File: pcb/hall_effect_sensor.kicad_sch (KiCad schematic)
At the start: 4 parts, among them U3 TMAG5273A2QDBV

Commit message: add top level schem and cleanup
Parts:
- renumbered C19 to C21, C18 to C22, R7 to R38, U3 to U5
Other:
- note removed: "1"
- note removed: "10/27/26"
- note removed: "Hall Effect w/ I2C connection"
- note removed: "Topher Fontana"
- title: (none) -> Hall Effect Sensor
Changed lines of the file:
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@@
 	(generator_version "10.0")
 	(paper "A4")
-	(text "10/27/26"
-		(exclude_from_sim no)
-		(at 212.598 193.294 0)
-		(effects
-			(font
-				(size 1.27 1.27)
-			)
-		)
-	)
-	(text "1"
-		(exclude_from_sim no)
-		(at 270.256 193.04 0)
-		(effects
-			(font
-				(size 1.27 1.27)
-			)
-		)
-	)
-	(text "Hall Effect w/ I2C connection"
-		(exclude_from_sim no)
-		(at 201.676 189.992 0)
-		(effects
-			(font
-				(size 1.27 1.27)
-			)
-		)
-	)
-	(text "Topher Fontana"
-		(exclude_from_sim no)
-		(at 194.056 174.244 0)
-		(effects
-			(font
-				(size 2.54 2.54)
-			)
-		)
+	(title_block
+		(title "Hall Effect Sensor")
+		(date "2026-10-27")
 	)
 	(junction
@@
 		)
 		(instances
+			(project "Onboard_Project"
+				(path "/17df1232-b180-49eb-a49c-63e4861e42e5/ac3adca3-c805-4f5b-864e-01bcaec77989"
+					(reference "#PWR060")
+					(unit 1)
+				)
+			)
+			(project "hall"
+				(path "/2f82c136-670b-48e5-bbb2-95c40d4f7cdb"
+					(reference "#PWR060")
+					(unit 1)
+				)
+			)
 			(project "Onboadrd_Project"
 				(path "/b0bfccf7-bea7-4d4b-a08d-f08cc4250cda"
@@
 		)
 		(instances
+			(project "Onboard_Project"
+				(path "/17df1232-b180-49eb-a49c-63e4861e42e5/ac3adca3-c805-4f5b-864e-01bcaec77989"
+					(reference "#PWR062")
+					(unit 1)
+				)
+			)
+			(project "hall"
+				(path "/2f82c136-670b-48e5-bbb2-95c40d4f7cdb"
+					(reference "#PWR062")
+					(unit 1)
+				)
+			)
 			(project "Onboadrd_Project"
 				(path "/b0bfccf7-bea7-4d4b-a08d-f08cc4250cda"
@@
 		)
 		(instances
+			(project "Onboard_Project"
+				(path "/17df1232-b180-49eb-a49c-63e4861e42e5/ac3adca3-c805-4f5b-864e-01bcaec77989"
+					(reference "#PWR058")
+					(unit 1)
+				)
+			)
+			(project "hall"
+				(path "/2f82c136-670b-48e5-bbb2-95c40d4f7cdb"
+					(reference "#PWR058")
+					(unit 1)
+				)
+			)
 			(project "Onboadrd_Project"
 				(path "/b0bfccf7-bea7-4d4b-a08d-f08cc4250cda"
@@
 		(in_pos_files yes)
 		(dnp no)
-		(property "Reference" "C19"
+		(property "Reference" "C21"
 			(at 161.29 68.58 0)
 			(show_name no)
@@
 		)
 		(instances
+			(project "Onboard_Project"
+				(path "/17df1232-b180-49eb-a49c-63e4861e42e5/ac3adca3-c805-4f5b-864e-01bcaec77989"
+					(reference "C21")
+					(unit 1)
+				)
+			)
+			(project "hall"
+				(path "/2f82c136-670b-48e5-bbb2-95c40d4f7cdb"
+					(reference "C22")
+					(unit 1)
+				)
+			)
 			(project "Onboadrd_Project"
 				(path "/b0bfccf7-bea7-4d4b-a08d-f08cc4250cda"
@@
 		)
 		(instances
+			(project "Onboard_Project"
+				(path "/17df1232-b180-49eb-a49c-63e4861e42e5/ac3adca3-c805-4f5b-864e-01bcaec77989"
+					(reference "#PWR061")
+					(unit 1)
+				)
+			)
+			(project "hall"
+				(path "/2f82c136-670b-48e5-bbb2-95c40d4f7cdb"
+					(reference "#PWR061")
+					(unit 1)
+				)
+			)
 			(project "Onboadrd_Project"
 				(path "/b0bfccf7-bea7-4d4b-a08d-f08cc4250cda"
@@
 		)
 		(instances
+			(project "Onboard_Project"
+				(path "/17df1232-b180-49eb-a49c-63e4861e42e5/ac3adca3-c805-4f5b-864e-01bcaec77989"
+					(reference "#PWR059")
+					(unit 1)
+				)
+			)
+			(project "hall"
+				(path "/2f82c136-670b-48e5-bbb2-95c40d4f7cdb"
+					(reference "#PWR059")
+					(unit 1)
+				)
+			)
 			(project "Onboadrd_Project"
 				(path "/b0bfccf7-bea7-4d4b-a08d-f08cc4250cda"
@@
 		(dnp no)
 		(fields_autoplaced yes)
-		(property "Reference" "R7"
+		(property "Reference" "R38"
 			(at 176.53 93.9799 0)
 			(show_name no)
@@
 		)
 		(instances
+			(project "Onboard_Project"
+				(path "/17df1232-b180-49eb-a49c-63e4861e42e5/ac3adca3-c805-4f5b-864e-01bcaec77989"
+					(reference "R38")
+					(unit 1)
+				)
+			)
+			(project "hall"
+				(path "/2f82c136-670b-48e5-bbb2-95c40d4f7cdb"
+					(reference "R36")
+					(unit 1)
+				)
+			)
 			(project "Onboadrd_Project"
 				(path "/b0bfccf7-bea7-4d4b-a08d-f08cc4250cda"
@@
 		(in_pos_files yes)
 		(dnp no)
-		(property "Reference" "U3"
+		(property "Reference" "U5"
 			(at 141.478 81.28 0)
 			(show_name no)
@@
 		)
 		(instances
+			(project "Onboard_Project"
+				(path "/17df1232-b180-49eb-a49c-63e4861e42e5/ac3adca3-c805-4f5b-864e-01bcaec77989"
+					(reference "U5")
+					(unit 1)
+				)
+			)
+			(project "hall"
+				(path "/2f82c136-670b-48e5-bbb2-95c40d4f7cdb"
+					(reference "U5")
+					(unit 1)
+				)
+			)
 			(project "Onboadrd_Project"
 				(path "/b0bfccf7-bea7-4d4b-a08d-f08cc4250cda"
@@
 		(dnp no)
 		(fields_autoplaced yes)
-		(property "Reference" "C18"
+		(property "Reference" "C22"
 			(at 161.2899 81.28 0)
 			(show_name no)
@@
 		)
 		(instances
+			(project "Onboard_Project"
+				(path "/17df1232-b180-49eb-a49c-63e4861e42e5/ac3adca3-c805-4f5b-864e-01bcaec77989"
+					(reference "C22")
+					(unit 1)
+				)
+			)
+			(project "hall"
+				(path "/2f82c136-670b-48e5-bbb2-95c40d4f7cdb"
+					(reference "C23")
+					(unit 1)
+				)
+			)
 			(project "Onboadrd_Project"
 				(path "/b0bfccf7-bea7-4d4b-a08d-f08cc4250cda"
@@
 		)
 	)
-	(sheet_instances
-		(path "/"
-			(page "4")
-		)
-	)

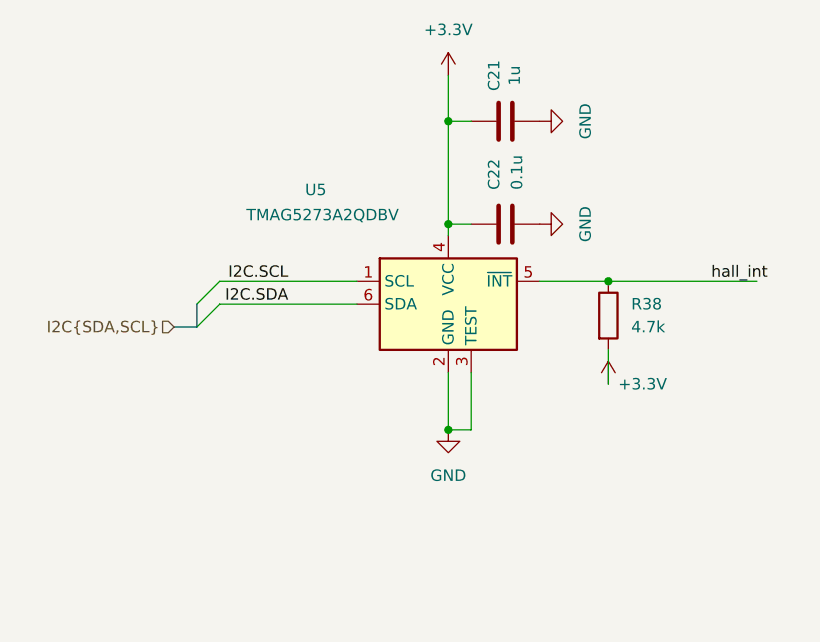
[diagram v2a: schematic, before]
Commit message: custom symbols for all ics
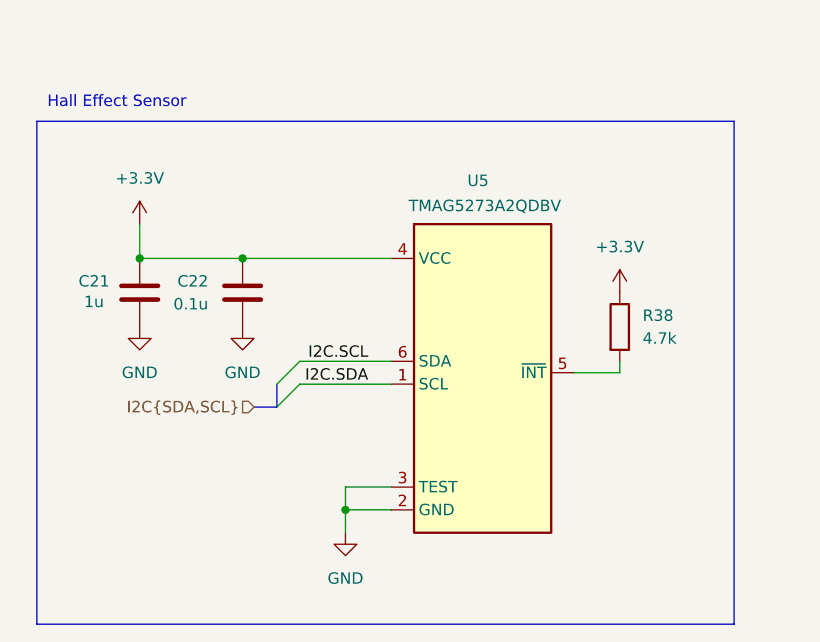
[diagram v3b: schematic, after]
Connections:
- net +3.3V: now also R38.1; no longer R38.2
- net I2C.SCL: now also U5.6 (SDA); no longer U5.1 (SCL)
- net I2C.SDA: now also U5.1 (SCL); no longer U5.6 (SDA)
- net hall_int: no longer names the net of U5.5 (~{INT})
- net hall_int: now also R38.2; no longer R38.1
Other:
- note added: "Hall Effect Sensor"
- moved on the sheet: R38, U5

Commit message: Adding some docs
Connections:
- net hall_int: now reaches R38.2, U5.5 (~{INT})

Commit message: Adding docs for GPIO and Color and removing INT
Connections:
- net hall_int: no longer names the net of R38.2, U5.5 (~{INT})
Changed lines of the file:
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@@
 	(title_block
 		(title "Hall Effect Sensor")
-		(date "2026-10-27")
+		(date "2026-10-28")
+		(rev "2")
 	)
 	(rectangle
@@
 	)
 	(junction
-		(at 175.26 101.6)
-		(diameter 0)
-		(color 0 0 0 0)
-	)
-	(junction
 		(at 133.35 88.9)
 		(diameter 0)
@@
 		(pts
 			(xy 133.35 88.9) (xy 149.86 88.9)
-		)
-		(stroke
-			(width 0)
-			(type default)
-		)
-	)
-	(wire
-		(pts
-			(xy 175.26 101.6) (xy 181.61 101.6)
 		)
 		(stroke
@@
 		)
 		(column_widths 21.59 36.83)
-		(row_heights 2.54 2.54 2.54 2.54 2.54 2.54 2.54)
+		(row_heights 2.54 2.54 2.54 2.54 2.54 2.54)
 		(cells
 			(table_cell "Device"
@@
 				(exclude_from_sim no)
 				(at 130.81 62.23 0)
-				(size 36.83 2.54)
-				(margins 0.9525 0.9525 0.9525 0.9525)
-				(span 1 1)
-				(fill
-					(type none)
-				)
-				(effects
-					(font
-						(size 1.27 1.27)
-					)
-					(justify left top)
-				)
-			)
-			(table_cell "Hall Int Pin"
-				(exclude_from_sim no)
-				(at 109.22 64.77 0)
-				(size 21.59 2.54)
-				(margins 0.9525 0.9525 0.9525 0.9525)
-				(span 1 1)
-				(fill
-					(type none)
-				)
-				(effects
-					(font
-						(size 1.27 1.27)
-					)
-					(justify left top)
-				)
-			)
-			(table_cell "RP2040 GPIO 0 (Pin 2)"
-				(exclude_from_sim no)
-				(at 130.81 64.77 0)
 				(size 36.83 2.54)
 				(margins 0.9525 0.9525 0.9525 0.9525)
@@
 		)
 	)
-	(hierarchical_label "hall_int"
-		(shape output)
-		(at 181.61 101.6 0)
-		(effects
-			(font
-				(size 1.27 1.27)
-			)
-			(justify left)
-		)
-	)
